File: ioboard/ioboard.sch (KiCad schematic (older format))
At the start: 20 parts

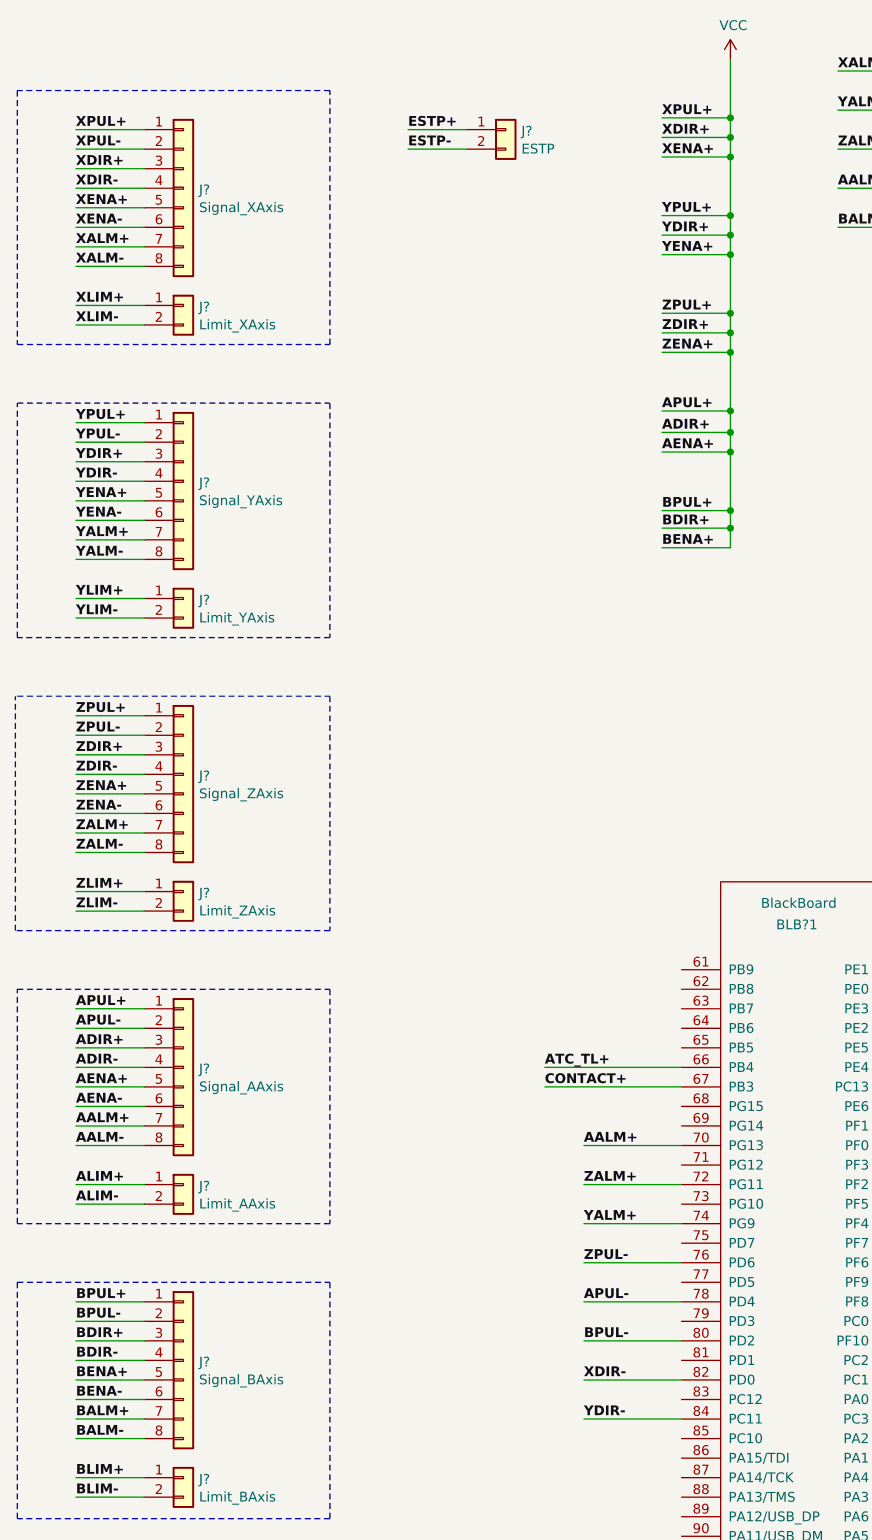
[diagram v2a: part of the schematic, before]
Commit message: spindle_control.stm32 module is compile-ready. pins have been shuffled around again the spindle timer will use the LL interface for its PWM signal because the HAL one is terrible and doesn't let you readjust on the fly, like anyone would want to with a PWM signal.
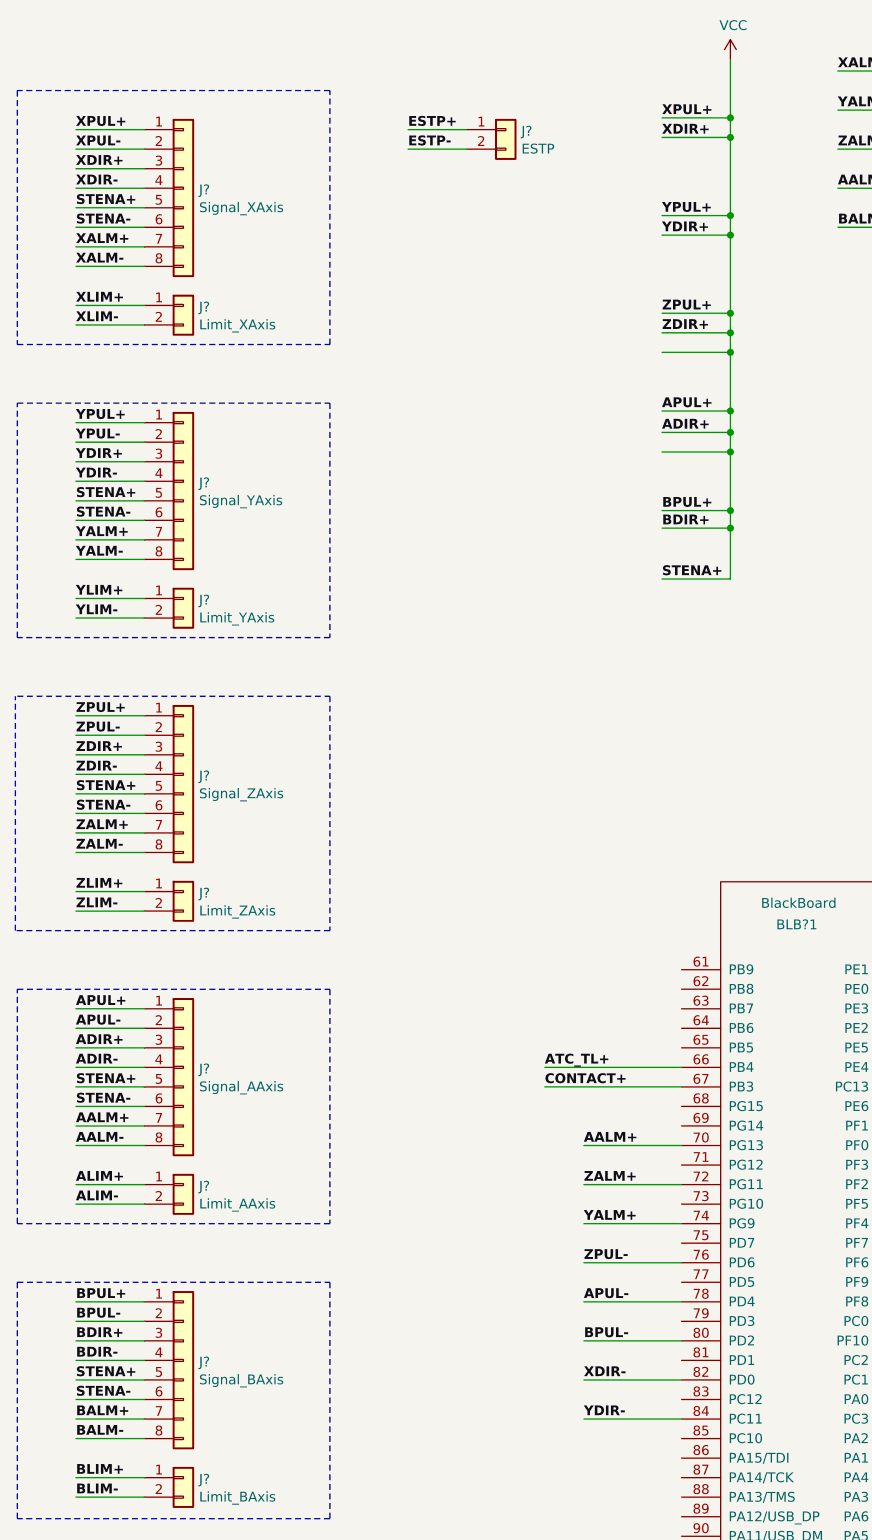
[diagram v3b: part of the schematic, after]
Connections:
- net AENA-: no longer J?.6 (Pin_6)
- net BENA-: no longer J?.6 (Pin_6)
- net XENA-: no longer J?.6 (Pin_6)
- net YENA-: no longer J?.6 (Pin_6)
- net ZENA-: no longer J?.6 (Pin_6)
- new net STENA-: J?.6 (Pin_6), J?.6 (Pin_6), J?.6 (Pin_6), J?.6 (Pin_6), J?.6 (Pin_6)
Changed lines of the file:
@@
 XDIR-
 Text Label 1700 1900 0    50   ~ 10
-XENA+
+STENA+
 Text Label 1700 2000 0    50   ~ 10
-XENA-
+STENA-
 Text Label 1700 2100 0    50   ~ 10
 XALM+
@@
 YDIR-
 Text Label 1700 3400 0    50   ~ 10
-YENA+
+STENA+
 Text Label 1700 3500 0    50   ~ 10
-YENA-
+STENA-
 Text Label 1700 3600 0    50   ~ 10
 YALM+
@@
 ZDIR-
 Text Label 1700 4900 0    50   ~ 10
-ZENA+
+STENA+
 Text Label 1700 5000 0    50   ~ 10
-ZENA-
+STENA-
 Text Label 1700 5100 0    50   ~ 10
 ZALM+
@@
 	6000 1200 5600 1200
 Wire Wire Line
-	5050 1640 4700 1640
-Wire Wire Line
 	4800 7900 4300 7900
 Wire Wire Line
@@
 Wire Wire Line
 	6000 1400 5600 1400
-Wire Wire Line
-	5050 2140 4700 2140
 Wire Wire Line
 	4800 8100 4300 8100
@@
 	5050 2640 5050 2540
 Connection ~ 5050 1540
-Connection ~ 5050 1640
-Wire Wire Line
-	5050 1640 5050 1540
 Connection ~ 5050 1940
-Wire Wire Line
-	5050 1940 5050 1640
 Connection ~ 5050 2040
 Wire Wire Line
 	5050 2040 5050 1940
-Connection ~ 5050 2140
-Wire Wire Line
-	5050 2140 5050 2040
 Connection ~ 5050 2440
-Wire Wire Line
-	5050 2440 5050 2140
 Connection ~ 5050 2540
 Wire Wire Line
@@
 ADIR-
 Text Label 1700 6400 0    50   ~ 10
-AENA+
+STENA+
 Text Label 1700 6500 0    50   ~ 10
-AENA-
+STENA-
 $Comp
 L Connector_Generic:Conn_01x08 J?
@@
 BDIR-
 Text Label 1700 7900 0    50   ~ 10
-BENA+
+STENA+
 Text Label 1700 8000 0    50   ~ 10
-BENA-
+STENA-
 Text Label 1700 8100 0    50   ~ 10
 BALM+
@@
 	6000 2000 5600 2000
 Wire Wire Line
-	5050 3640 4700 3640
-Wire Wire Line
 	6000 9100 6500 9100
 Wire Wire Line
@@
 Text Label 5600 2000 0    50   ~ 10
 BALM-
-Wire Wire Line
-	5050 3640 5050 3540
 Connection ~ 5050 2640
 Connection ~ 5050 2940
@@
 Wire Wire Line
 	11780 1600 11580 1600
-Text Label 4700 3640 0    50   ~ 10
-BENA+
 Text Label 4700 3540 0    50   ~ 10
 BDIR+
 Text Label 4700 3450 0    50   ~ 10
 BPUL+
-Text Label 4700 3150 0    50   ~ 10
-AENA+
 Text Label 4700 3050 0    50   ~ 10
 ADIR+
 Text Label 4700 2940 0    50   ~ 10
 APUL+
-Text Label 4700 2640 0    50   ~ 10
-ZENA+
 Text Label 4700 2540 0    50   ~ 10
 ZDIR+
 Text Label 4700 2440 0    50   ~ 10
 ZPUL+
-Text Label 4700 2140 0    50   ~ 10
-YENA+
 Text Label 4700 2040 0    50   ~ 10
 YDIR+
 Text Label 4700 1940 0    50   ~ 10
 YPUL+
-Text Label 4700 1640 0    50   ~ 10
-XENA+
 Text Label 4700 1540 0    50   ~ 10
 XDIR+
@@
 Wire Wire Line
 	2050 9950 1740 9950
+Wire Wire Line
+	5050 1540 5050 1940
+Wire Wire Line
+	5050 2040 5050 2440
+Text Label 4700 3800 0    50   ~ 10
+STENA+
+Wire Wire Line
+	5050 3800 4700 3800
+Wire Wire Line
+	5050 3540 5050 3800
 $EndSCHEMATC

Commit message: coolant control is compile-ready
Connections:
- net MIST is gone; now on net MIST+: BLB?1.53 (PB11)
- net FLOOD+: now also BLB?1.54 (PB10)
- net SPDIR: now also J?.4 (Pin_4)
- net SPEN: now also J?.3 (Pin_3)
- net AENA-: no longer names the net of BLB?1.15 (PF7)
- net BENA-: no longer names the net of BLB?1.17 (PF9)
- net XENA- renamed STEN-
- net YENA-: no longer names the net of BLB?1.11 (PF3)
- net ZENA-: no longer names the net of BLB?1.13 (PF5)
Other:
- moved on the sheet: J?
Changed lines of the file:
@@
 Wire Wire Line
 	6000 6400 6490 6400
-Text Label 7200 6800 2    50   ~ 10
+Text Label 3460 4870 0    50   ~ 10
 SPPWM
 Wire Wire Line
 	6000 6200 6500 6200
 Text Label 6500 6600 2    50   ~ 10
-XENA-
-Text Label 6510 6800 2    50   ~ 10
-YENA-
-Text Label 6500 7000 2    50   ~ 10
-ZENA-
-Text Label 6500 7200 2    50   ~ 10
-AENA-
-Text Label 6500 7400 2    50   ~ 10
-BENA-
+STEN-
 Text Label 4400 11600 0    50   ~ 0
 VCC
@@
 Wire Wire Line
 	6000 6600 6500 6600
-Wire Wire Line
-	6000 6800 6510 6800
-Wire Wire Line
-	6000 7000 6500 7000
-Wire Wire Line
-	6000 7200 6500 7200
-Wire Wire Line
-	6000 7400 6500 7400
 $Comp
 L power:VCC #PWR?
@@
 L Connector_Generic:Conn_01x04 J?
 U 1 1 61140DCB
-P 10000 4000
-F 0 "J?" H 10080 3992 50  0000 L CNN
-F 1 "SpindleCOMM" H 10080 3901 50  0000 L CNN
-F 2 "" H 10000 4000 50  0001 C CNN
-F 3 "~" H 10000 4000 50  0001 C CNN
-	1    10000 4000
-	1    0    0    -1
-$EndComp
-Text Label 9300 3900 0    50   ~ 10
+P 4150 4540
+F 0 "J?" H 4230 4532 50  0000 L CNN
+F 1 "SpindleCOMM" H 4230 4441 50  0000 L CNN
+F 2 "" H 4150 4540 50  0001 C CNN
+F 3 "~" H 4150 4540 50  0001 C CNN
+	1    4150 4540
+	1    0    0    -1
+$EndComp
+Text Label 3450 4440 0    50   ~ 10
 SPSPD
-Text Label 9300 4000 0    50   ~ 10
+Text Label 3450 4540 0    50   ~ 10
 ACOM
 Wire Wire Line
-	9300 3900 9800 3900
-Wire Wire Line
-	9300 4000 9800 4000
+	3450 4440 3950 4440
+Wire Wire Line
+	3450 4540 3950 4540
 Text Label 6500 6500 2    50   ~ 10
 XLIM+
@@
 ATC_TL+
 Text Label 6500 11000 2    50   ~ 10
-MIST
+MIST+
 Wire Wire Line
 	6500 11000 6000 11000
@@
 Wire Wire Line
 	5050 3540 5050 3800
+Text Label 3450 4640 0    50   ~ 10
+SPEN
+Text Label 3450 4740 0    50   ~ 10
+SPDIR
+Wire Wire Line
+	3950 4640 3450 4640
+Wire Wire Line
+	3450 4740 3950 4740
+Text Label 6490 11100 2    50   ~ 10
+FLOOD+
+Wire Wire Line
+	6490 11100 6000 11100
 $EndSCHEMATC
